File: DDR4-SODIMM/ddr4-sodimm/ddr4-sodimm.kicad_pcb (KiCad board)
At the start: 6 copper layers, 69.6 x 30 mm, 1 part

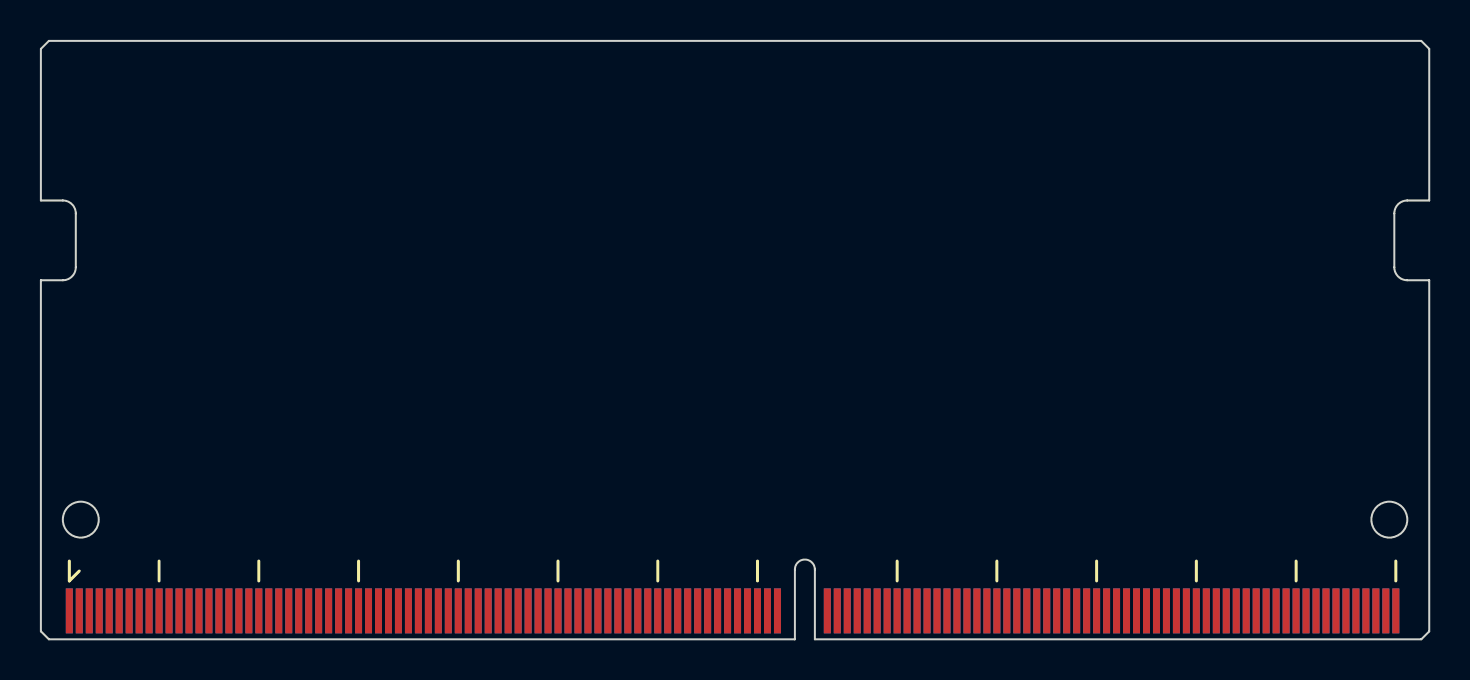
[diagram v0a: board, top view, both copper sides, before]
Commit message: correct back side for pin2 ~ pin260
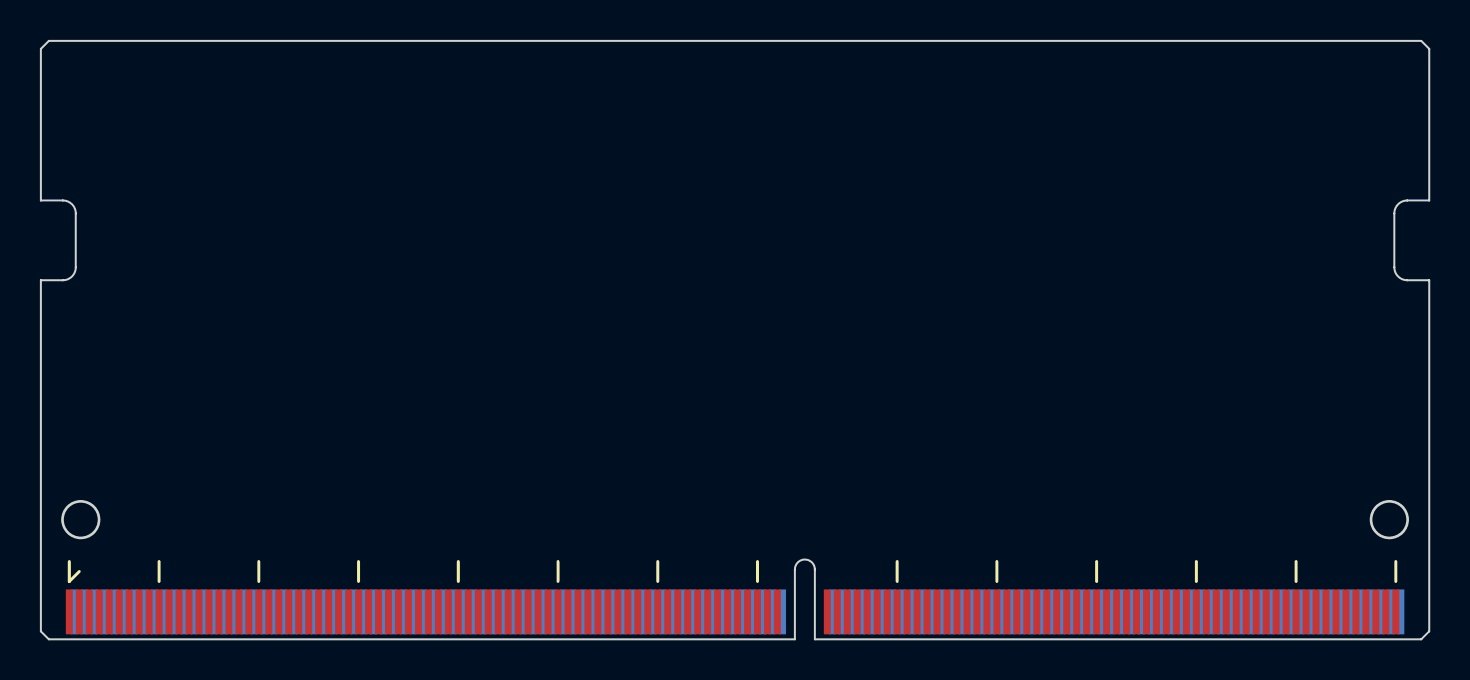
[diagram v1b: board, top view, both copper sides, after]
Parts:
- moved REF** 2.02 mm to (100.0, 100.0)
